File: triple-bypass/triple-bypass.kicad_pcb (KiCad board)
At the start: 2 copper layers, 32 x 39.4 mm, 70 parts, among them CON101 MD-90SM, J101 HDR1X2, J102 JMP-PCB-3POS, U101 THS7374IPWR, U102 LMV358M8G-13

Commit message: First commit
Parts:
- removed 0V1, 5V1, B1, G1, S1, SL1, SN1, SR2, XL1, XR2, YL1, YR2: TP_50, db-smt:TP50
- removed C100, C116, C117: 0.1uF/50V, db-smt:0603
- removed C101: 220uF/10V, db-smt:SMD-6.6x6.6
- removed C102, C109, C110: 10uF/10V, db-smt:0805
- removed C103, C104, C105, C106, C107, C108: 1uF/16V, db-smt:0603
- removed C111, C112: 270pF/50V, db-smt:0603
- removed C113, C114, C115: 22uF/10V, db-smt:1206_P
- removed CON101: MD-90SM, db-thparts:MD-90SM
- removed G***: LOGO, db-artwork:oshw-logo_5mm
- removed G***: LOGO, db-artwork:db-logo_7.5mm
- removed J101: HDR1X2, db-thparts:HDR1X2
- removed J102: JMP-PCB-3POS, db-smt:JMP-PCB-3POS
- removed R102, R113, R119: 2.20k, db-smt:0603
- removed R103, R104, R105, R106: 5.62k, db-smt:0603
- removed R107, R108, R109, R110: 1.00k, db-smt:0603
- removed R111, R123, R124: 100k, db-smt:0603
- removed R112, R114, R115, R117, R118: 75.0, db-smt:0603
- removed R116: 1.30k, db-smt:0603
- removed R120, R127: 6.19k, db-smt:0603
- removed R121, R122, R125, R126: 130k, db-smt:0603
- removed R128, R129: 10.0k, db-smt:0603
- removed R130, R131: 162k, db-smt:0603
- removed R132, R133: 332, db-smt:0603
- removed U101: THS7374IPWR, db-smt:TSSOP-14
- removed U102: LMV358M8G-13, db-smt:TSSOP-8_3.0mm
- added C1: 10uF/10V, Capacitor_SMD:C_0603_1608Metric, F.Cu at (126.6, 111.6)
- added C10: 180pF/50V, Capacitor_SMD:C_0603_1608Metric, F.Cu at (137.6, 93.1)
- added C11: 180pF/50V, Capacitor_SMD:C_0603_1608Metric, F.Cu at (145.6, 93.1)
- added C12: 10uF/10V, Capacitor_SMD:C_0603_1608Metric, F.Cu at (139.6, 89.1)
- added C13: 0.1uF/50V, Capacitor_SMD:C_0603_1608Metric, F.Cu at (140.1, 95.6)
- added C14: 22uF/10V, Capacitor_Tantalum_SMD:CP_EIA-3216-18_Kemet-A_Pad1.58x1.35mm_HandSolder, F.Cu at (135.6, 90.1)
- added C15: 22uF/10V, Capacitor_Tantalum_SMD:CP_EIA-3216-18_Kemet-A_Pad1.58x1.35mm_HandSolder, F.Cu at (147.6, 90.1)
- added C16: 22uF/10V, Capacitor_Tantalum_SMD:CP_EIA-3216-18_Kemet-A_Pad1.58x1.35mm_HandSolder, F.Cu at (150.3, 65.4)
- added C17: 0.1uF/50V, Capacitor_SMD:C_0603_1608Metric, F.Cu at (147.6, 65.1)
- added C18: 220uF/10V, Capacitor_SMD:CP_Elec_6.3x5.4_Nichicon, F.Cu at (141.6, 80.1)
- added C2: 10uF/10V, Capacitor_SMD:C_0603_1608Metric, F.Cu at (156.6, 111.6)
- added C3: 1uF/16V, Capacitor_SMD:C_0603_1608Metric, F.Cu at (130.6, 111.6)
- added C4: 1uF/16V, Capacitor_SMD:C_0603_1608Metric, F.Cu at (152.6, 111.6)
- added C5: 1uF/16V, Capacitor_SMD:C_0603_1608Metric, F.Cu at (134.6, 111.6)
- added C6: 1uF/16V, Capacitor_SMD:C_0603_1608Metric, F.Cu at (148.6, 111.6)
- added C8: 1uF/16V, Capacitor_SMD:C_0603_1608Metric, F.Cu at (138.6, 111.6)
- added C9: 1uF/16V, Capacitor_SMD:C_0603_1608Metric, F.Cu at (144.6, 111.6)
- added FD1: Fiducial, Fiducial:Fiducial_0.5mm_Dia_1mm_Outer, F.Cu at (138.6, 115.6)
- added FD2: Fiducial, Fiducial:Fiducial_0.5mm_Dia_1mm_Outer, F.Cu at (130.8, 66.1)
- added FD3: Fiducial, Fiducial:Fiducial_0.5mm_Dia_1mm_Outer, F.Cu at (154.1, 66.6)
- added J1: MD-90SM, CUI_MD-90SM, B.Cu at (134.6, 66.4)
- added JP1: SolderJumper_3_Open, Jumper:SolderJumper-2_P1.3mm_Open_RoundedPad1.0x1.5mm, F.Cu at (128.6, 106.1)
- added JP10: SolderJumper_3_Open, Jumper:SolderJumper-2_P1.3mm_Open_RoundedPad1.0x1.5mm, F.Cu at (127.6, 97.1)
- added JP11: SolderJumper_3_Open, Jumper:SolderJumper-2_P1.3mm_Open_RoundedPad1.0x1.5mm, F.Cu at (155.6, 89.1)
- added JP12: SolderJumper_3_Open, Jumper:SolderJumper-2_P1.3mm_Open_RoundedPad1.0x1.5mm, F.Cu at (155.6, 93.1)
- added JP13: SolderJumper_3_Open, Jumper:SolderJumper-2_P1.3mm_Open_RoundedPad1.0x1.5mm, F.Cu at (155.6, 97.1)
- added JP14: SolderJumper_3_Open, Jumper:SolderJumper-2_P1.3mm_Open_RoundedPad1.0x1.5mm, F.Cu at (142.6, 105.1)
- added JP2: SolderJumper_3_Open, Jumper:SolderJumper-2_P1.3mm_Open_RoundedPad1.0x1.5mm, F.Cu at (154.6, 106.1)
- added JP3: SolderJumper_3_Open, Jumper:SolderJumper-2_P1.3mm_Open_RoundedPad1.0x1.5mm, F.Cu at (132.6, 106.1)
- added JP4: SolderJumper_3_Open, Jumper:SolderJumper-2_P1.3mm_Open_RoundedPad1.0x1.5mm, F.Cu at (150.6, 106.1)
- added JP5: SolderJumper_3_Open, Jumper:SolderJumper-2_P1.3mm_Open_RoundedPad1.0x1.5mm, F.Cu at (136.6, 106.1)
- added JP6: SolderJumper_3_Open, Jumper:SolderJumper-2_P1.3mm_Open_RoundedPad1.0x1.5mm, F.Cu at (146.6, 106.1)
- added JP7: SolderJumper_3_Open, Jumper:SolderJumper-2_P1.3mm_Open_RoundedPad1.0x1.5mm, F.Cu at (140.6, 105.1)
- added JP8: SolderJumper_3_Open, Jumper:SolderJumper-2_P1.3mm_Open_RoundedPad1.0x1.5mm, F.Cu at (127.6, 89.1)
- added JP9: SolderJumper_3_Open, Jumper:SolderJumper-2_P1.3mm_Open_RoundedPad1.0x1.5mm, F.Cu at (127.6, 93.1)
- added LOGO1: Logo_Open_Hardware_Small, Symbol:OSHW-Logo2_7.3x6mm_SilkScreen, B.Cu at (141.6, 106.6)
- added P1: TP_50, TestPoint:TestPoint_Pad_1.5x1.5mm, F.Cu at (129.1, 83.6)
- added P10: TP_50, TestPoint:TestPoint_Pad_1.5x1.5mm, F.Cu at (147.6, 114.6)
- added P11: TP_50, TestPoint:TestPoint_Pad_1.5x1.5mm, F.Cu at (131.6, 114.6)
- added P12: TP_50, TestPoint:TestPoint_Pad_1.5x1.5mm, F.Cu at (151.6, 114.6)
- added P13: TP_50, TestPoint:TestPoint_Pad_1.5x1.5mm, F.Cu at (141.6, 114.6)
- added P2: TP_50, TestPoint:TestPoint_Pad_1.5x1.5mm, F.Cu at (129.1, 77.1)
- added P3: TP_50, TestPoint:TestPoint_Pad_1.5x1.5mm, F.Cu at (155.1, 79.6)
- added P4: TP_50, TestPoint:TestPoint_Pad_1.5x1.5mm, F.Cu at (155.1, 76.1)
- added P5: TP_50, TestPoint:TestPoint_Pad_1.5x1.5mm, F.Cu at (155.1, 72.6)
- added P6: TP_50, TestPoint:TestPoint_Pad_1.5x1.5mm, F.Cu at (155.1, 83.1)
- added P7: TP_50, TestPoint:TestPoint_Pad_1.5x1.5mm, F.Cu at (127.6, 114.6)
- added P8: TP_50, TestPoint:TestPoint_Pad_1.5x1.5mm, F.Cu at (155.6, 114.6)
- added P9: TP_50, TestPoint:TestPoint_Pad_1.5x1.5mm, F.Cu at (135.6, 114.6)
- added R10: 130K, Resistor_SMD:R_0603_1608Metric, F.Cu at (148.6, 106.1)
- added R11: 6K19, Resistor_SMD:R_0603_1608Metric, F.Cu at (131.1, 89.6)
- added R12: 43K, Resistor_SMD:R_0603_1608Metric, F.Cu at (131.1, 93.6)
- added R13: 56K, Resistor_SMD:R_0603_1608Metric, F.Cu at (131.1, 97.6)
- added R14: 750R, Resistor_SMD:R_0603_1608Metric, F.Cu at (140.6, 111.6)
- added R15: 2K2, Resistor_SMD:R_0603_1608Metric, F.Cu at (142.6, 111.6)
- added R16: 6K19, Resistor_SMD:R_0603_1608Metric, F.Cu at (152.1, 89.6)
- added R17: 43K, Resistor_SMD:R_0603_1608Metric, F.Cu at (152.1, 93.6)
- added R18: 56K, Resistor_SMD:R_0603_1608Metric, F.Cu at (152.1, 97.6)
- added R19: 120K, Resistor_SMD:R_0603_1608Metric, F.Cu at (138.6, 106.1)
- added R2: 2K2, Resistor_SMD:R_0603_1608Metric, F.Cu at (154.6, 111.6)
- added R20: 120K, Resistor_SMD:R_0603_1608Metric, F.Cu at (144.6, 106.1)
- added R21: 240K, Resistor_SMD:R_0603_1608Metric, F.Cu at (135.6, 93.1)
- added R22: 240K, Resistor_SMD:R_0603_1608Metric, F.Cu at (147.6, 93.1)
- added R23: 10K, Resistor_SMD:R_0603_1608Metric, F.Cu at (141.6, 89.1)
- added R24: 10K, Resistor_SMD:R_0603_1608Metric, F.Cu at (143.6, 89.1)
- added R25: 332R, Resistor_SMD:R_0603_1608Metric, F.Cu at (133.6, 93.1)
- added R26: 332R, Resistor_SMD:R_0603_1608Metric, F.Cu at (149.6, 93.1)
- added R27: 2K2, Resistor_SMD:R_0603_1608Metric, F.Cu at (152.8, 83.1)
- added R28: 5K62, Resistor_SMD:R_0603_1608Metric, F.Cu at (149.1, 82.4)
- added R29: 5K62, Resistor_SMD:R_0603_1608Metric, F.Cu at (152.8, 79.9)
- added R3: 75R, Resistor_SMD:R_0603_1608Metric, F.Cu at (132.6, 111.6)
- added R30: 5K62, Resistor_SMD:R_0603_1608Metric, F.Cu at (152.8, 76.4)
- added R31: 5K62, Resistor_SMD:R_0603_1608Metric, F.Cu at (152.8, 72.9)
- added R32: 1K, Resistor_SMD:R_0603_1608Metric, F.Cu at (149.1, 84.1)
- added R33: 1K, Resistor_SMD:R_0603_1608Metric, F.Cu at (151.1, 79.9)
- added R34: 1K, Resistor_SMD:R_0603_1608Metric, F.Cu at (151.1, 76.4)
- added R35: 1K, Resistor_SMD:R_0603_1608Metric, F.Cu at (151.1, 72.9)
- added R36: 100K, Resistor_SMD:R_0603_1608Metric, F.Cu at (151.1, 68.9)
- added R37: 75R, Resistor_SMD:R_0603_1608Metric, F.Cu at (141.6, 75.1)
- added R4: 75R, Resistor_SMD:R_0603_1608Metric, F.Cu at (150.6, 111.6)
- added R5: 75R, Resistor_SMD:R_0603_1608Metric, F.Cu at (136.6, 111.6)
- added R6: 75R, Resistor_SMD:R_0603_1608Metric, F.Cu at (146.6, 111.6)
- added R7: 130K, Resistor_SMD:R_0603_1608Metric, F.Cu at (130.6, 106.1)
- added R8: 130K, Resistor_SMD:R_0603_1608Metric, F.Cu at (152.6, 106.1)
- added R9: 130K, Resistor_SMD:R_0603_1608Metric, F.Cu at (134.6, 106.1)
- added SW2: SW_SPDT, 100:CL-SB-12B-01, F.Cu at (154.6, 66.9)
- added SW3: SW_SPDT, 100:CL-SB-12B-01, F.Cu at (133.6, 80.1)
- added U1: LMV358M8G-13, Package_SO:TSSOP-8_3x3mm_P0.65mm, F.Cu at (141.6, 93.1)
- added U2: THS7374IPWR, Package_SO:TSSOP-14_4.4x5mm_P0.65mm, F.Cu at (146.6, 70.9)
- R1: value TP_50 -> 2K2; footprint db-smt:TP50 -> Resistor_SMD:R_0603_1608Metric
- moved R1 23.0 mm to (128.6, 111.6), turned to 90 degrees
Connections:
- R1 pad 1: /R-In -> /Mega Amp/YM-LEFT-IN
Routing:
- net /Mega Amp/R-CH: track 0.00 -> 51.9 mm
- net /Mega Amp/L-CH: track 0.00 -> 51.3 mm
- net GND: track 90.0 -> 50.8 mm, vias 18 -> 22
- net /SR: track 3.74 -> 38.6 mm, vias 0 -> 2
- net /SYNC-TTL: track 34.1 -> 0.00 mm, vias 2 -> 0
- net /SL: track 3.89 -> 32.9 mm
- net /Video Amp/SYNC-IN: track 0.00 -> 26.1 mm
- net Net-(C2-Pad1): track 0.00 -> 21.9 mm
- net Net-(C1-Pad1): track 0.00 -> 21.9 mm
- net +5V: track 84.1 -> 104.5 mm, vias 3 -> 4
- net Net-(C112-Pad1): track 18.8 -> 0.00 mm
- net Net-(C110-Pad2): track 18.1 -> 0.00 mm
- net Net-(C111-Pad1): track 18.1 -> 0.00 mm
- net Net-(C111-Pad2): track 16.1 -> 0.00 mm
- net Net-(SW2-Pad2): track 0.00 -> 14.1 mm, vias 0 -> 2
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- removed copper zone on F.Cu, net GND
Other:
- board size 32 x 39.4 mm -> 33 x 56 mm
- net class Power: clearance 0.1778 -> 0.254; trace_width 0.254 -> 0.3048; via_dia 0.6096 -> 0.8128
- board text added: "2612"
- board text added: "2K2"
- board text added: "32L"
- board text added: "32R"
- board text added: "32X75"
- board text added: "750"
- board text added: "75R"
- board text added: "ASIC"
- board text added: "CD75"
- board text added: "CDL"
- board text added: "CDR"
- board text added: "GOAC"
- board text added: "LEFT-CH"
- board text added: "LPF"
- board text added: "ON"
- board text added: "PULLDOWNS"
- board text added: "RIGHT-CH"
- board text added: "SYNC"
- board text added: "TRIPLE BYPASS AIO"
- board text added: "TTL"
- board text added: "YM2K2"
- board text added: "YML"
- board text added: "YMR"
- board text added: "v0.4"
- board text removed: "CL"
- board text removed: "CR"
- board text removed: "S"
- board text removed: "XL"
- board text removed: "XR"
- board text removed: "YL"
- board text removed: "YR"
- board text removed: "db-electronics.ca"
- board text removed: "triple bypass"
- board text removed: "v0.3"

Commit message: Organize and export pdf
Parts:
- moved SW3 1.00 mm to (132.6, 80.1)
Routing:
- net /Video Amp/SYNC-IN: track 26.1 -> 27.1 mm
- net /SYNC-75: track 10.7 -> 11.5 mm

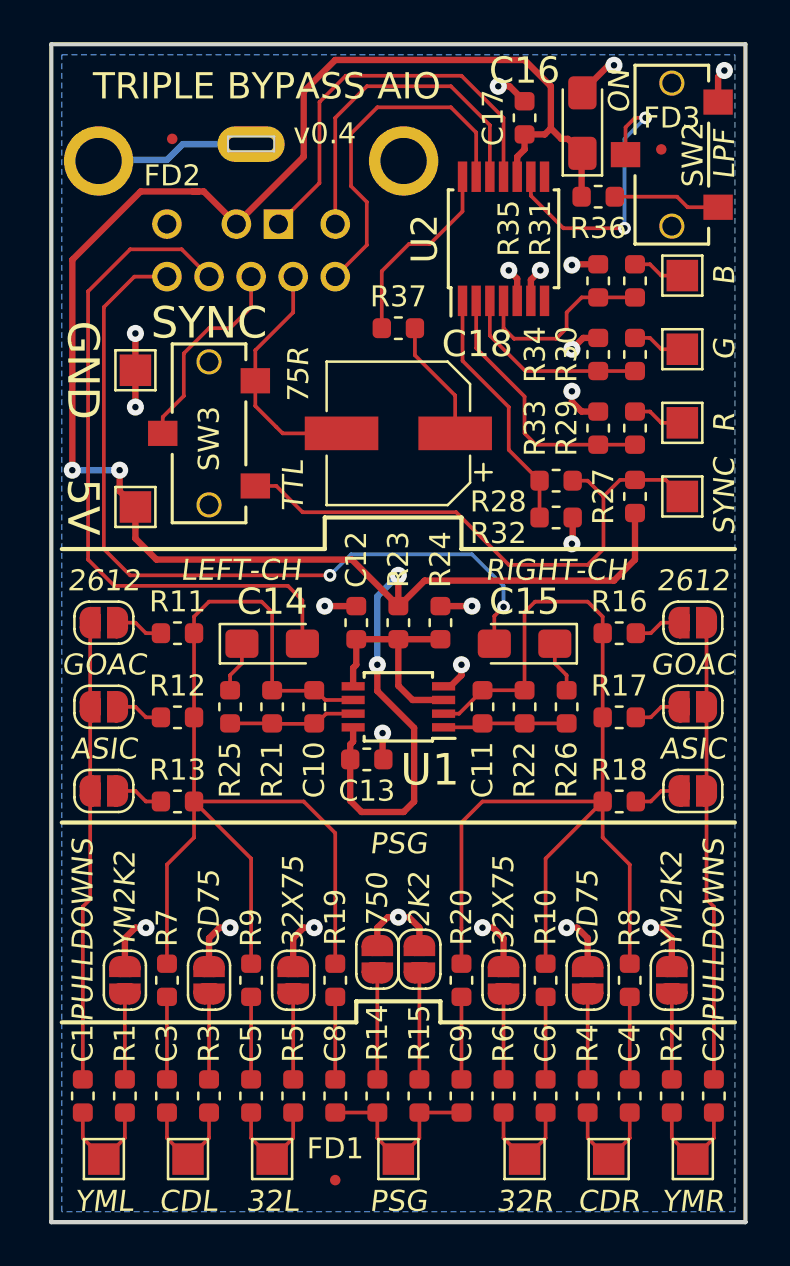
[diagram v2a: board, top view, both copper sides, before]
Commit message: Increase 5V rail width
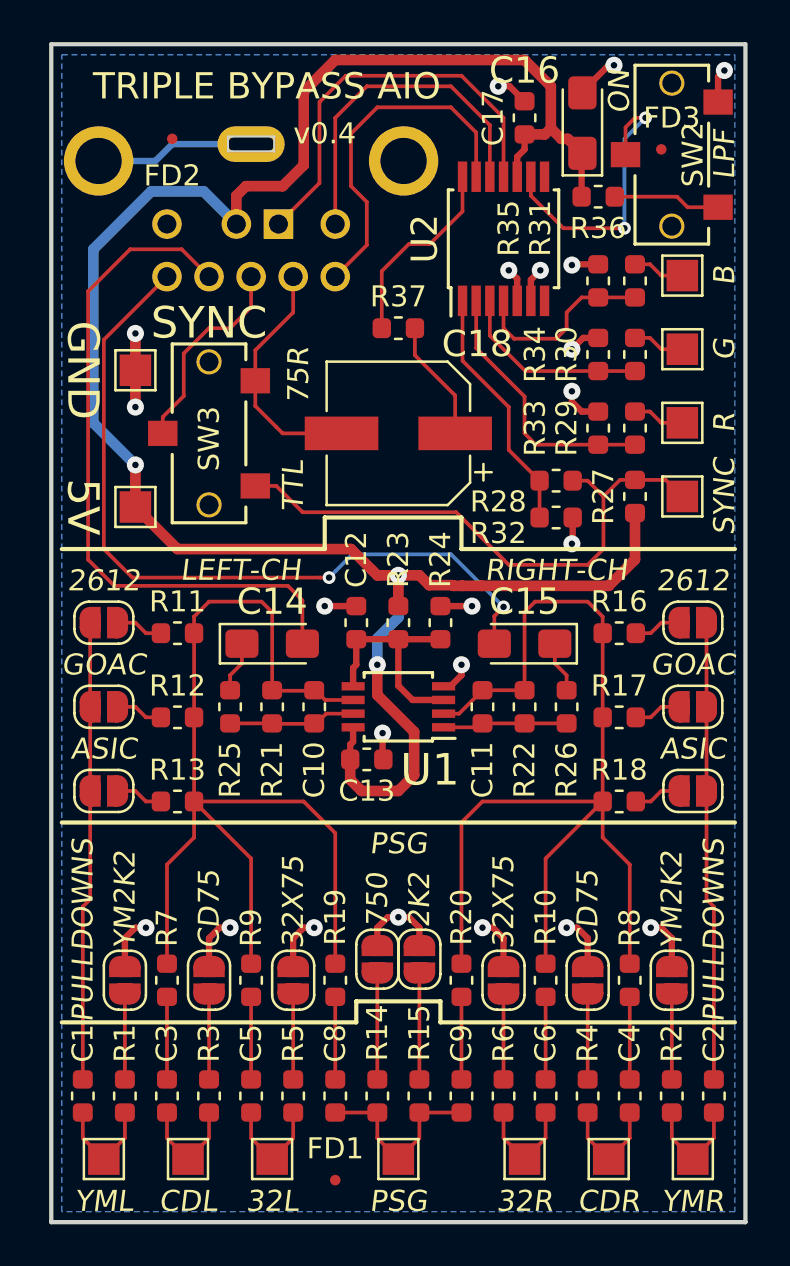
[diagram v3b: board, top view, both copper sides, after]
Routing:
- net +5V: track 104.5 -> 99.0 mm, vias 4 -> 3
- net /SR: track 38.6 -> 37.2 mm
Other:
- net class 5V added: clearance 0.3048, trace_width 0.508, via_dia 0.8128, via_drill 0.3048
